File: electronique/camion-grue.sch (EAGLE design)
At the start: 91 parts, among them P1 RGEF800, Q1 BSS138, Q2 BSS138, U1 TEENSY_3.5_DIL+USB, U2 TEENSY_3.1-3.2_DIL

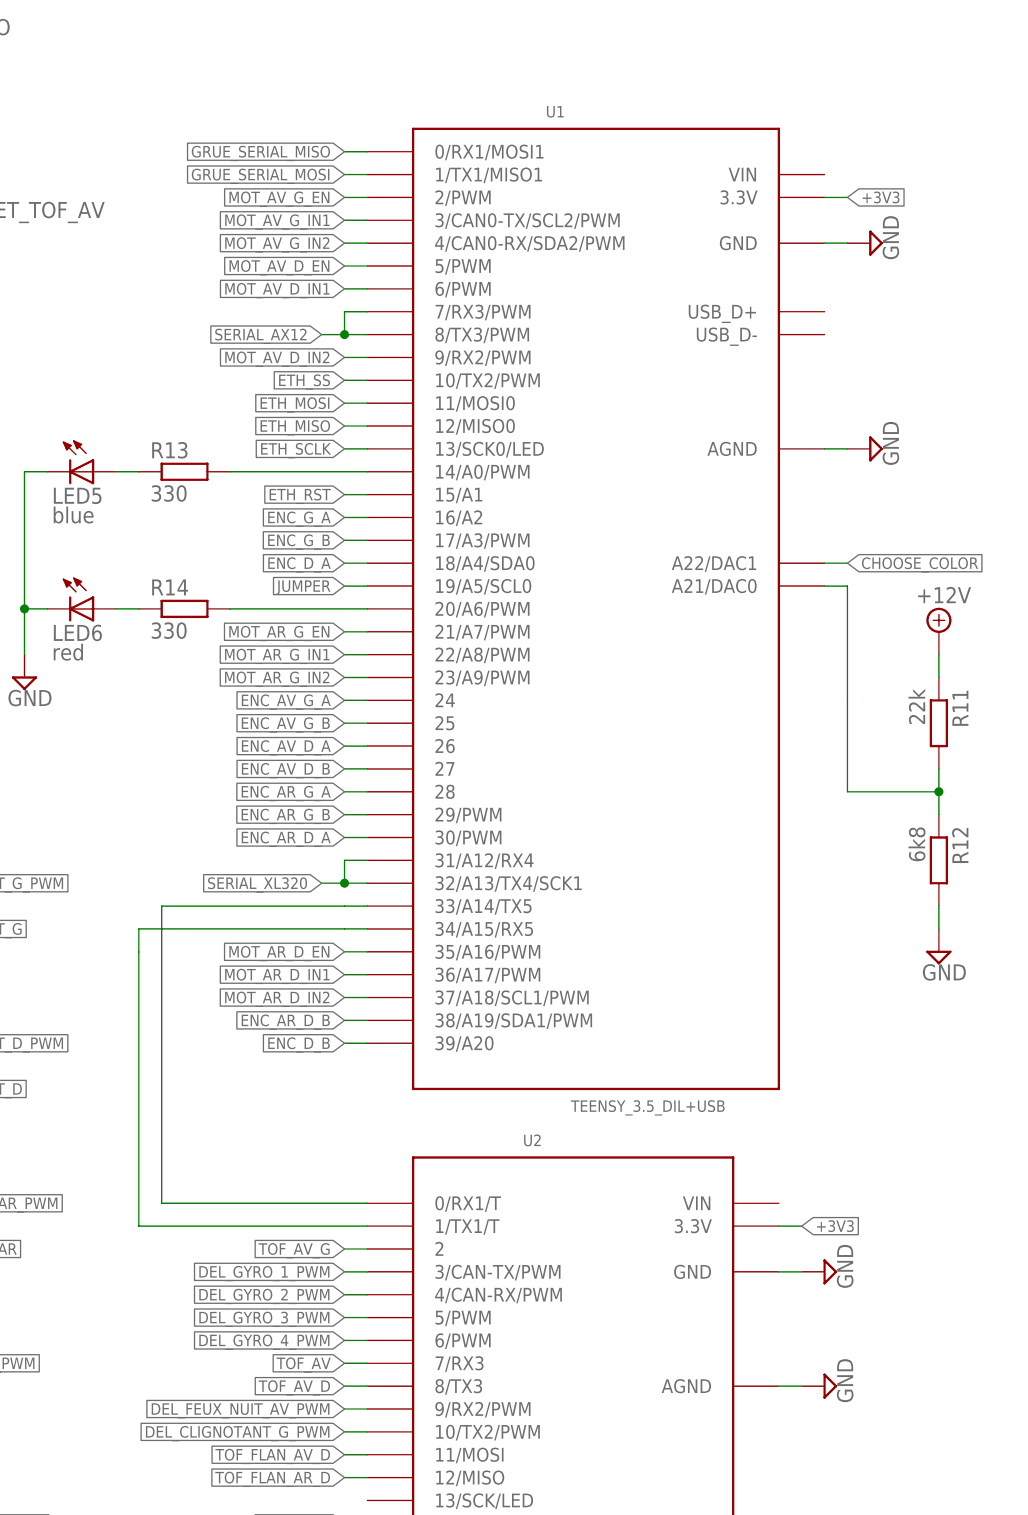
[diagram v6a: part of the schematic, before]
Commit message: Elec: routage catre principale presque fini !
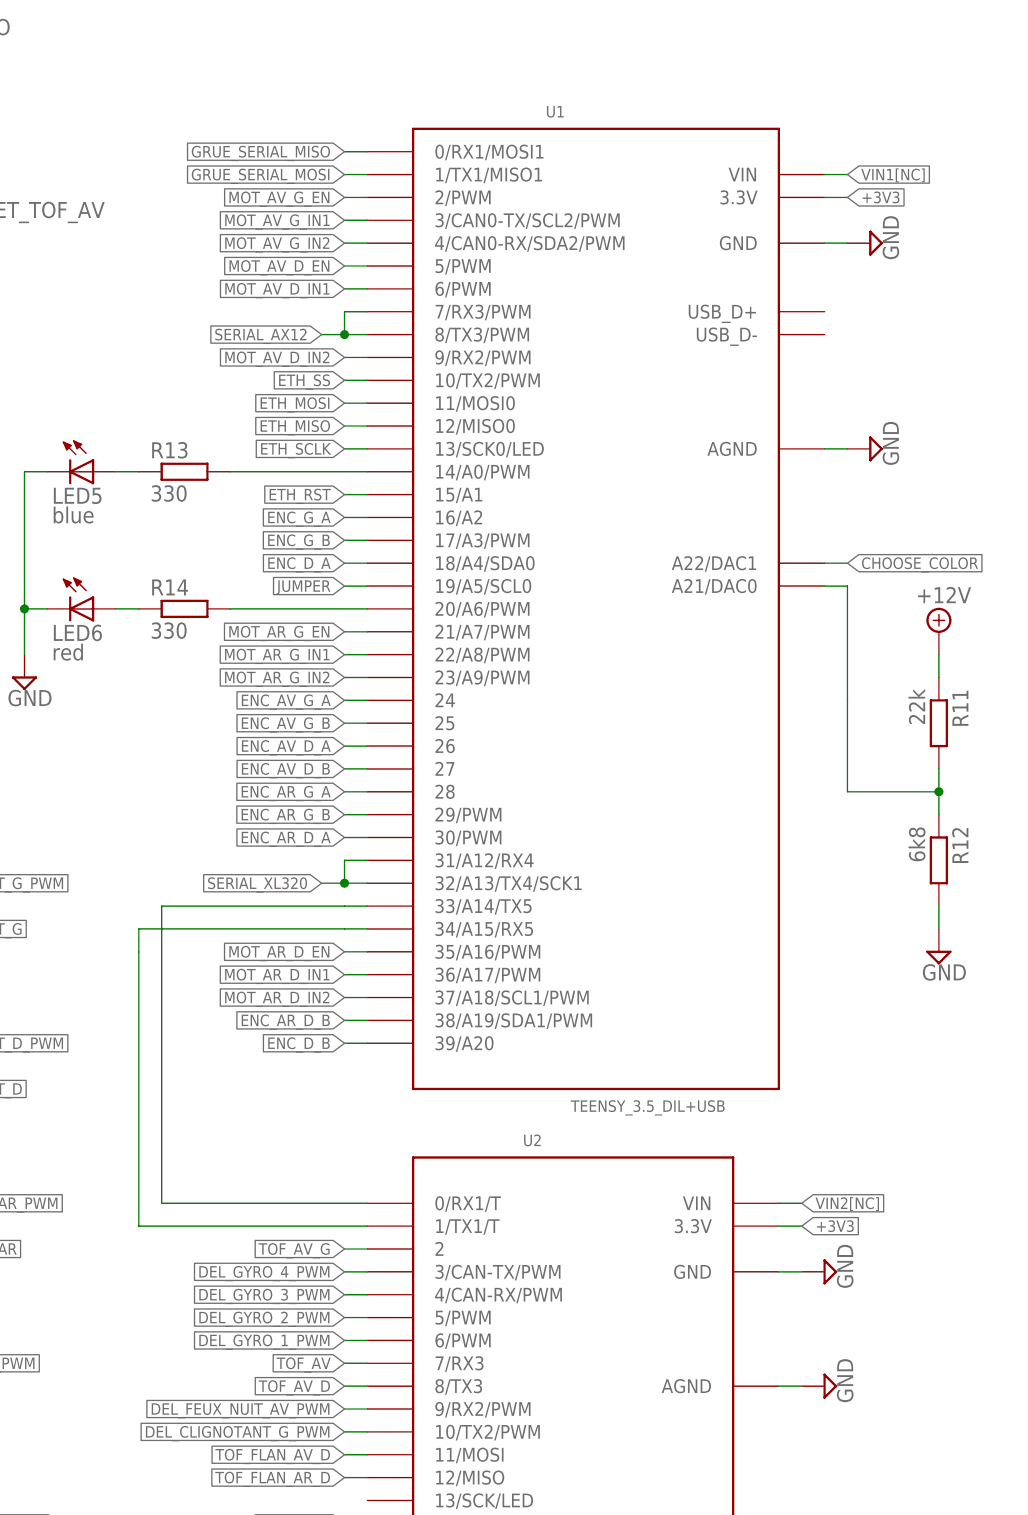
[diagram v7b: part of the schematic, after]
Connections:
- new net VIN1[NC]: U1.VIN
- new net VIN2[NC]: U2.VIN
- net DEL_GYRO_1_PWM: now also U2.6/PWM; no longer U2.3/CAN-TX/PWM
- net DEL_GYRO_2_PWM: now also U2.5/PWM; no longer U2.4/CAN-RX/PWM
- net DEL_GYRO_3_PWM: now also U2.4/CAN-RX/PWM; no longer U2.5/PWM
- net DEL_GYRO_4_PWM: now also U2.3/CAN-TX/PWM; no longer U2.6/PWM
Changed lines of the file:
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@@
 <net name="DEL_GYRO_3_PWM" class="0">
+<segment>
+<pinref part="R18" gate="G$1" pin="1"/>
+<wire x1="203.2" y1="114.3" x2="205.74" y2="114.3" width="0.1524" layer="91"/>
+<label x="205.74" y="114.3" size="1.27" layer="95" xref="yes"/>
+</segment>
+<segment>
+<pinref part="U2" gate="G$1" pin="4/CAN-RX/PWM"/>
+<wire x1="312.42" y1="104.14" x2="309.88" y2="104.14" width="0.1524" layer="91"/>
+<label x="309.88" y="104.14" size="1.27" layer="95" rot="R180" xref="yes"/>
+</segment>
+</net>
+<net name="DEL_GYRO_4_PWM" class="0">
+<segment>
+<pinref part="R21" gate="G$1" pin="1"/>
+<wire x1="203.2" y1="96.52" x2="205.74" y2="96.52" width="0.1524" layer="91"/>
+<label x="205.74" y="96.52" size="1.27" layer="95" xref="yes"/>
+</segment>
+<segment>
+<pinref part="U2" gate="G$1" pin="3/CAN-TX/PWM"/>
+<wire x1="312.42" y1="106.68" x2="309.88" y2="106.68" width="0.1524" layer="91"/>
+<label x="309.88" y="106.68" size="1.27" layer="95" rot="R180" xref="yes"/>
+</segment>
+</net>
+<net name="DEL_FEUX_NUIT_AV_PWM" class="0">
+<segment>
+<pinref part="U2" gate="G$1" pin="9/RX2/PWM"/>
+<wire x1="312.42" y1="91.44" x2="309.88" y2="91.44" width="0.1524" layer="91"/>
+<label x="309.88" y="91.44" size="1.27" layer="95" rot="R180" xref="yes"/>
+</segment>
+<segment>
+<pinref part="R23" gate="G$1" pin="1"/>
+<wire x1="203.2" y1="78.74" x2="205.74" y2="78.74" width="0.1524" layer="91"/>
+<label x="205.74" y="78.74" size="1.27" layer="95" xref="yes"/>
+</segment>
+</net>
+<net name="DEL_CLIGNOTANT_G_PWM" class="0">
+<segment>
+<pinref part="U2" gate="G$1" pin="10/TX2/PWM"/>
+<wire x1="312.42" y1="88.9" x2="309.88" y2="88.9" width="0.1524" layer="91"/>
+<label x="309.88" y="88.9" size="1.27" layer="95" rot="R180" xref="yes"/>
+</segment>
+<segment>
+<pinref part="R25" gate="G$1" pin="1"/>
+<wire x1="254" y1="149.86" x2="256.54" y2="149.86" width="0.1524" layer="91"/>
+<label x="256.54" y="149.86" size="1.27" layer="95" xref="yes"/>
+</segment>
+</net>
+<net name="DEL_CLIGNOTANT_D_PWM" class="0">
+<segment>
+<pinref part="U2" gate="G$1" pin="20/A6/PWM"/>
+<wire x1="312.42" y1="63.5" x2="309.88" y2="63.5" width="0.1524" layer="91"/>
+<label x="309.88" y="63.5" size="1.27" layer="95" rot="R180" xref="yes"/>
+</segment>
+<segment>
+<pinref part="R27" gate="G$1" pin="1"/>
+<wire x1="254" y1="132.08" x2="256.54" y2="132.08" width="0.1524" layer="91"/>
+<label x="256.54" y="132.08" size="1.27" layer="95" xref="yes"/>
+</segment>
+</net>
+<net name="DEL_GYRO_1_PWM" class="0">
+<segment>
+<pinref part="R19" gate="G$1" pin="1"/>
+<wire x1="203.2" y1="149.86" x2="205.74" y2="149.86" width="0.1524" layer="91"/>
+<label x="205.74" y="149.86" size="1.27" layer="95" xref="yes"/>
+</segment>
+<segment>
+<pinref part="U2" gate="G$1" pin="6/PWM"/>
+<wire x1="312.42" y1="99.06" x2="309.88" y2="99.06" width="0.1524" layer="91"/>
+<label x="309.88" y="99.06" size="1.27" layer="95" rot="R180" xref="yes"/>
+</segment>
+</net>
+<net name="DEL_GYRO_2_PWM" class="0">
+<segment>
+<pinref part="R16" gate="G$1" pin="1"/>
+<wire x1="203.2" y1="132.08" x2="205.74" y2="132.08" width="0.1524" layer="91"/>
+<label x="205.74" y="132.08" size="1.27" layer="95" xref="yes"/>
+</segment>
 <segment>
 <pinref part="U2" gate="G$1" pin="5/PWM"/>
@@
 <label x="309.88" y="101.6" size="1.27" layer="95" rot="R180" xref="yes"/>
 </segment>
-<segment>
-<pinref part="R18" gate="G$1" pin="1"/>
-<wire x1="203.2" y1="114.3" x2="205.74" y2="114.3" width="0.1524" layer="91"/>
-<label x="205.74" y="114.3" size="1.27" layer="95" xref="yes"/>
-</segment>
-</net>
-<net name="DEL_GYRO_4_PWM" class="0">
-<segment>
-<pinref part="U2" gate="G$1" pin="6/PWM"/>
-<wire x1="312.42" y1="99.06" x2="309.88" y2="99.06" width="0.1524" layer="91"/>
-<label x="309.88" y="99.06" size="1.27" layer="95" rot="R180" xref="yes"/>
-</segment>
-<segment>
-<pinref part="R21" gate="G$1" pin="1"/>
-<wire x1="203.2" y1="96.52" x2="205.74" y2="96.52" width="0.1524" layer="91"/>
-<label x="205.74" y="96.52" size="1.27" layer="95" xref="yes"/>
-</segment>
-</net>
-<net name="DEL_FEUX_NUIT_AV_PWM" class="0">
-<segment>
-<pinref part="U2" gate="G$1" pin="9/RX2/PWM"/>
-<wire x1="312.42" y1="91.44" x2="309.88" y2="91.44" width="0.1524" layer="91"/>
-<label x="309.88" y="91.44" size="1.27" layer="95" rot="R180" xref="yes"/>
-</segment>
-<segment>
-<pinref part="R23" gate="G$1" pin="1"/>
-<wire x1="203.2" y1="78.74" x2="205.74" y2="78.74" width="0.1524" layer="91"/>
-<label x="205.74" y="78.74" size="1.27" layer="95" xref="yes"/>
-</segment>
-</net>
-<net name="DEL_CLIGNOTANT_G_PWM" class="0">
-<segment>
-<pinref part="U2" gate="G$1" pin="10/TX2/PWM"/>
-<wire x1="312.42" y1="88.9" x2="309.88" y2="88.9" width="0.1524" layer="91"/>
-<label x="309.88" y="88.9" size="1.27" layer="95" rot="R180" xref="yes"/>
-</segment>
-<segment>
-<pinref part="R25" gate="G$1" pin="1"/>
-<wire x1="254" y1="149.86" x2="256.54" y2="149.86" width="0.1524" layer="91"/>
-<label x="256.54" y="149.86" size="1.27" layer="95" xref="yes"/>
-</segment>
-</net>
-<net name="DEL_CLIGNOTANT_D_PWM" class="0">
-<segment>
-<pinref part="U2" gate="G$1" pin="20/A6/PWM"/>
-<wire x1="312.42" y1="63.5" x2="309.88" y2="63.5" width="0.1524" layer="91"/>
-<label x="309.88" y="63.5" size="1.27" layer="95" rot="R180" xref="yes"/>
-</segment>
-<segment>
-<pinref part="R27" gate="G$1" pin="1"/>
-<wire x1="254" y1="132.08" x2="256.54" y2="132.08" width="0.1524" layer="91"/>
-<label x="256.54" y="132.08" size="1.27" layer="95" xref="yes"/>
-</segment>
-</net>
-<net name="DEL_GYRO_1_PWM" class="0">
-<segment>
-<pinref part="U2" gate="G$1" pin="3/CAN-TX/PWM"/>
-<wire x1="312.42" y1="106.68" x2="309.88" y2="106.68" width="0.1524" layer="91"/>
-<label x="309.88" y="106.68" size="1.27" layer="95" rot="R180" xref="yes"/>
-</segment>
-<segment>
-<pinref part="R19" gate="G$1" pin="1"/>
-<wire x1="203.2" y1="149.86" x2="205.74" y2="149.86" width="0.1524" layer="91"/>
-<label x="205.74" y="149.86" size="1.27" layer="95" xref="yes"/>
-</segment>
-</net>
-<net name="DEL_GYRO_2_PWM" class="0">
-<segment>
-<pinref part="U2" gate="G$1" pin="4/CAN-RX/PWM"/>
-<wire x1="312.42" y1="104.14" x2="309.88" y2="104.14" width="0.1524" layer="91"/>
-<label x="309.88" y="104.14" size="1.27" layer="95" rot="R180" xref="yes"/>
-</segment>
-<segment>
-<pinref part="R16" gate="G$1" pin="1"/>
-<wire x1="203.2" y1="132.08" x2="205.74" y2="132.08" width="0.1524" layer="91"/>
-<label x="205.74" y="132.08" size="1.27" layer="95" xref="yes"/>
-</segment>
 </net>
 <net name="DEL_FEUX_NUIT_AR_PWM" class="0">
@@
 </segment>
 </net>
+<net name="VIN1[NC]" class="0">
+<segment>
+<pinref part="U1" gate="G$1" pin="VIN"/>
+<wire x1="363.22" y1="228.6" x2="365.76" y2="228.6" width="0.1524" layer="91"/>
+<label x="365.76" y="228.6" size="1.27" layer="95" xref="yes"/>
+</segment>
+</net>
+<net name="VIN2[NC]" class="0">
+<segment>
+<pinref part="U2" gate="G$1" pin="VIN"/>
+<wire x1="358.14" y1="114.3" x2="360.68" y2="114.3" width="0.1524" layer="91"/>
+<label x="360.68" y="114.3" size="1.27" layer="95" xref="yes"/>
+</segment>
+</net>

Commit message: Elec cockpit terminée
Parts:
- added USB_BACKUP_DEBUG: (no value), pinhead:PINHD-1X3
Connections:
- new net USB_D+: U1.USB_D+, USB_BACKUP_DEBUG.2
- new net USB_D-: U1.USB_D-, USB_BACKUP_DEBUG.3
- net GND: now also USB_BACKUP_DEBUG.1
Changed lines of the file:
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@@
 <part name="SUPPLY71" library="supply2" library_urn="urn:adsk.eagle:library:372" deviceset="GND" device=""/>
 <part name="SUPPLY72" library="supply2" library_urn="urn:adsk.eagle:library:372" deviceset="GND" device=""/>
+<part name="USB_BACKUP_DEBUG" library="pinhead" library_urn="urn:adsk.eagle:library:325" deviceset="PINHD-1X3" device="" package3d_urn="urn:adsk.eagle:package:22458/2"/>
+<part name="SUPPLY73" library="supply2" library_urn="urn:adsk.eagle:library:372" deviceset="GND" device=""/>
 </parts>
 <sheets>
@@
 <instance part="SUPPLY71" gate="GND" x="93.98" y="78.74"/>
 <instance part="SUPPLY72" gate="GND" x="109.22" y="78.74"/>
+<instance part="USB_BACKUP_DEBUG" gate="A" x="340.36" y="35.56"/>
+<instance part="SUPPLY73" gate="GND" x="330.2" y="40.64" rot="R180"/>
 </instances>
 <busses>
@@
 <pinref part="SUPPLY72" gate="GND" pin="GND"/>
 <wire x1="109.22" y1="81.28" x2="106.68" y2="81.28" width="0.1524" layer="91"/>
+</segment>
+<segment>
+<pinref part="USB_BACKUP_DEBUG" gate="A" pin="1"/>
+<wire x1="337.82" y1="38.1" x2="330.2" y2="38.1" width="0.1524" layer="91"/>
+<pinref part="SUPPLY73" gate="GND" pin="GND"/>
 </segment>
 </net>
@@
 </segment>
 </net>
+<net name="USB_D+" class="0">
+<segment>
+<pinref part="U1" gate="G$1" pin="USB_D+"/>
+<wire x1="363.22" y1="213.36" x2="365.76" y2="213.36" width="0.1524" layer="91"/>
+<label x="365.76" y="213.36" size="1.27" layer="95" xref="yes"/>
+</segment>
+<segment>
+<pinref part="USB_BACKUP_DEBUG" gate="A" pin="2"/>
+<wire x1="337.82" y1="35.56" x2="332.74" y2="35.56" width="0.1524" layer="91"/>
+<label x="332.74" y="35.56" size="1.27" layer="95" rot="R180" xref="yes"/>
+</segment>
+</net>
+<net name="USB_D-" class="0">
+<segment>
+<pinref part="U1" gate="G$1" pin="USB_D-"/>
+<wire x1="363.22" y1="210.82" x2="365.76" y2="210.82" width="0.1524" layer="91"/>
+<label x="365.76" y="210.82" size="1.27" layer="95" xref="yes"/>
+</segment>
+<segment>
+<pinref part="USB_BACKUP_DEBUG" gate="A" pin="3"/>
+<wire x1="337.82" y1="33.02" x2="332.74" y2="33.02" width="0.1524" layer="91"/>
+<label x="332.74" y="33.02" size="1.27" layer="95" rot="R180" xref="yes"/>
+</segment>
+</net>
